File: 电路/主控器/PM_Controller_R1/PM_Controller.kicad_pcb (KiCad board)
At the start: 4 copper layers, 90 x 61.5 mm, 134 parts, among them J1 Conn_01x04_Socket, J10 Conn_02x04_Odd_Even, J11 Conn_02x06_Odd_Even, J2 Conn_01x04_Socket, J3 Conn_01x04_Socket, J4 Conn_01x04_Socket, J5 Conn_01x02_Pin, J6 Conn_01x02_Pin, J7 Conn_02x04_Odd_Even, J8 Conn_01x04_Pin, J9 Conn_01x04_Socket, P2V5 SolderJumper_2_Open, P3V3 SolderJumper_2_Open, Q1 AO3401A, Q2 AO3400A, Q3 AO3400A, Q4 AO3400A, Q5 AO3400A, Q6 AO3400A, U1 AT24CS08-SSHM, U10 TMP102xxDRL, U11 TPS2552DDBVR, U12 TLP127, U2 AMS1117-3.3, U3 STM32G431RBTx, U4 TPS61085DGK, U5 BQ21040DBV, U6 TPS2552DDBVR, U7 STM32L011D4Px, U8 ME6211C25M5, U9 AT24CS08-SSHM, Y1 32.768kHz, Y2 24Mhz

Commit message: Rev1.0版本可正常工作
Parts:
- added C39: 100nf, Capacitor_SMD:C_0603_1608Metric_Pad1.08x0.95mm_HandSolder, F.Cu at (61.1, 119.5)
- added C40: 22uf, Capacitor_Tantalum_SMD:CP_EIA-3528-21_Kemet-B_HandSolder, F.Cu at (69.7, 119.5)
- added C41: 100nf, Capacitor_SMD:C_0603_1608Metric_Pad1.08x0.95mm_HandSolder, F.Cu at (64.2, 126.2)
- added R43: 22k, Resistor_SMD:R_0603_1608Metric_Pad0.98x0.95mm_HandSolder, F.Cu at (64.5, 122.7)
- added R44: 100k, Resistor_SMD:R_0603_1608Metric_Pad0.98x0.95mm_HandSolder, F.Cu at (61.1, 123.1)
- added U13: TPS2552DDBVR, KiCadLib:DBV0006A_TEX, F.Cu at (64.1, 120.0)
- added U14: ADUM3201ARZ-RL7, ADUM3201:R_8_ADI, B.Cu at (64.3, 121.9)
- R42: value 100k -> 1k
- R7: moved to F.Cu
- moved CHG1 17.9 mm to (50.1, 158.0), turned to 0 degrees
- moved PW_LED1 17.6 mm to (50.1, 160.4), turned to 0 degrees
- moved R42 9.00 mm to (58.5, 118.0), turned to 90 degrees
- moved R4 5.38 mm to (60.8, 161.8)
- moved C16 4.36 mm to (50.8, 155.0), turned to -90 degrees
- moved J8 2.91 mm to (67.0, 115.2)
- moved R7 1.60 mm to (64.4, 165.6)
- moved J9 1.58 mm to (69.4, 124.8)
- moved R9 1.02 mm to (53.2, 156.0)
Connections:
- J8 pad 1: +3.3V -> /LASER_3.3V
- J8 pad 2: /TX2 -> /TX2_o
- J8 pad 3: /RX2 -> /RX2_o
- U3 pad 10: unconnected-(U3-PC2-Pad10) -> /SDM_EN
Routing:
- net /SDM_EN: track 0.00 -> 46.7 mm, vias 0 -> 2
- net Net-(PW_LED1-A): track 22.3 -> 39.0 mm
- net GND: track 101.2 -> 112.5 mm, vias 100 -> 106
- net Net-(J6-Pin_2): track 10.4 -> 2.01 mm
- net +3.3V: track 38.8 -> 46.6 mm, vias 25 -> 28
- net /LASER_3.3V: track 0.00 -> 7.16 mm, vias 0 -> 1
- net /RX2: track 42.4 -> 36.4 mm
- net /#CHRG: track 15.5 -> 21.0 mm
- net /RX2_o: track 0.00 -> 5.01 mm, vias 0 -> 1
- net /TX2_o: track 0.00 -> 4.78 mm
- net Net-(U13-ILIM): track 0.00 -> 3.86 mm
- net Net-(CHG1-A): track 6.69 -> 10.3 mm
- net +BATT: track 14.0 -> 17.3 mm
- net /TX2: track 44.6 -> 41.4 mm
- net /PWR_LED: track 22.2 -> 25.3 mm
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- added copper zone on F.Cu, net /LASER_3.3V
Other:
- board size 90 x 61.5 mm -> 89.5 x 61.5 mm

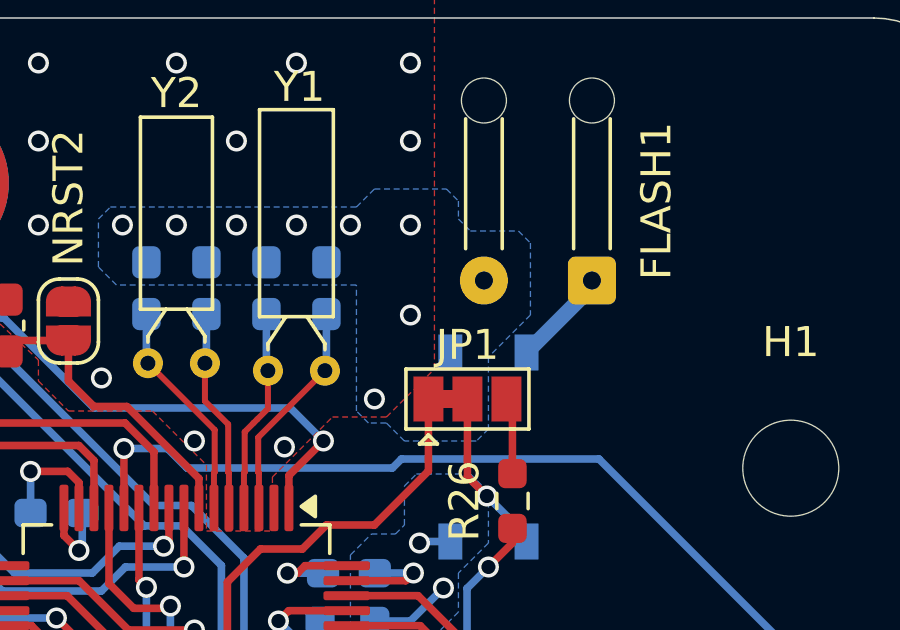
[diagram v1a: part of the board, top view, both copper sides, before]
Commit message: 闪关灯功能OK 准备给电机加一个斜坡
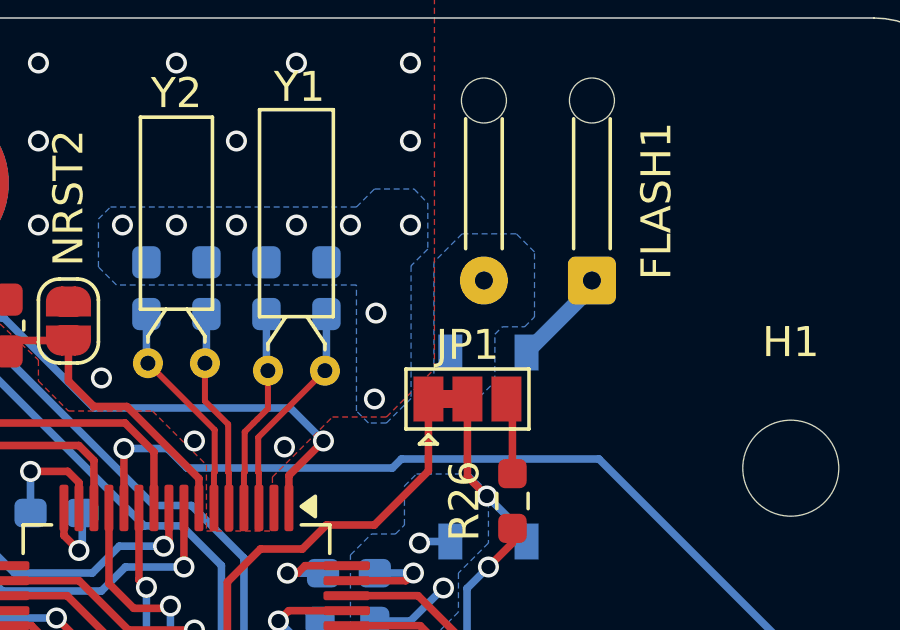
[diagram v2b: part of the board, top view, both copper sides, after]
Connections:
- FLASH1 pad 2: GND -> /FLASH_Trig_Return
- U12 pad 4: GND -> /FLASH_Trig_Return
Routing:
- added copper zone on B.Cu, net /FLASH_Trig_Return
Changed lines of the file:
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@@
 	(net 113 "/TX2_o")
 	(net 114 "/RX2_o")
+	(net 115 "/FLASH_Trig_Return")
 	(footprint "Connector_PinHeader_1.27mm:PinHeader_2x04_P1.27mm_Vertical"
 		(locked yes)
@@
 			(layers "*.Cu" "*.Mask")
 			(remove_unused_layers no)
-			(net 7 "GND")
+			(net 115 "/FLASH_Trig_Return")
 			(pinfunction "Pin_2")
 			(pintype "passive")
@@
 		(fp_text user "*"
 			(at -0.4953 -1.4478 0)
+			(unlocked yes)
 			(layer "F.Fab")
 			(effects
@@
 		(fp_text user "*"
 			(at -0.4953 -1.4478 0)
-			(unlocked yes)
 			(layer "F.Fab")
 			(effects
@@
 		(fp_text user "*"
 			(at -1.4478 2.6518 0)
+			(unlocked yes)
 			(layer "B.SilkS")
 			(effects
@@
 		(fp_text user "*"
 			(at -1.4478 2.6518 0)
-			(unlocked yes)
 			(layer "B.SilkS")
 			(effects
@@
 		(fp_text user "*"
 			(at -0.4953 1.4478 0)
+			(unlocked yes)
 			(layer "B.Fab")
 			(effects
@@
 		(fp_text user "*"
 			(at -0.4953 1.4478 0)
-			(unlocked yes)
 			(layer "B.Fab")
 			(effects
@@
 			(size 1.2 0.8)
 			(layers "B.Cu" "B.Mask" "B.Paste")
-			(net 7 "GND")
+			(net 115 "/FLASH_Trig_Return")
 			(pintype "passive")
 		)
@@
 	)
 	(via
-		(at 110.186092 123.4)
+		(at 109.038492 123.3364)
 		(size 0.7)
 		(drill 0.47)
@@
 		(polygon
 			(pts
-				(xy 111.786092 119.6) (xy 111.786092 120.2) (xy 112.186092 120.6) (xy 113.786092 120.6) (xy 114.186092 121)
-				(xy 114.186092 123.4) (xy 112.786092 124.8) (xy 112.786092 127.2) (xy 112.386092 127.6) (xy 109.986092 127.6)
+				(xy 110.765692 119.6788) (xy 110.765692 121.2028) (xy 110.206892 121.7616) (xy 110.206892 126.1812)
 				(xy 109.386092 127) (xy 108.786092 127) (xy 108.386092 126.6) (xy 108.386092 122.4) (xy 100.386092 122.4)
 				(xy 99.786092 121.8) (xy 99.786092 120.2) (xy 100.186092 119.8) (xy 108.386092 119.8) (xy 108.986092 119.2)
-				(xy 111.386092 119.2)
+				(xy 110.308492 119.2)
 			)
 		)
@@
 			)
 		)
+	)
+	(zone
+		(net 115)
+		(net_name "/FLASH_Trig_Return")
+		(layer "B.Cu")
+		(hatch edge 0.5)
+		(priority 36)
+		(connect_pads
+			(clearance 0.5)
+		)
+		(min_thickness 0.25)
+		(filled_areas_thickness no)
+		(fill yes
+			(thermal_gap 0.3)
+			(thermal_bridge_width 0.5)
+		)
+		(polygon
+			(pts
+				(xy 110.968892 125.7494) (xy 111.349892 126.1304) (xy 112.492892 126.1304) (xy 113.000892 125.6224)
+				(xy 113.000892 124.04125) (xy 113.248542 123.7936) (xy 113.991492 123.7936) (xy 114.321692 123.4634)
+				(xy 114.321692 121.29805) (xy 113.718442 120.6948) (xy 111.908692 120.6948) (xy 110.968892 121.6346)
+			)
+		)
